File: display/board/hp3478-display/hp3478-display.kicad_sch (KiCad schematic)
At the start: 60 parts, among them J1 Header, J2 Header, U1 FT60F1x2, U2 SM16206S, U3 74HC595, U4 74HC595

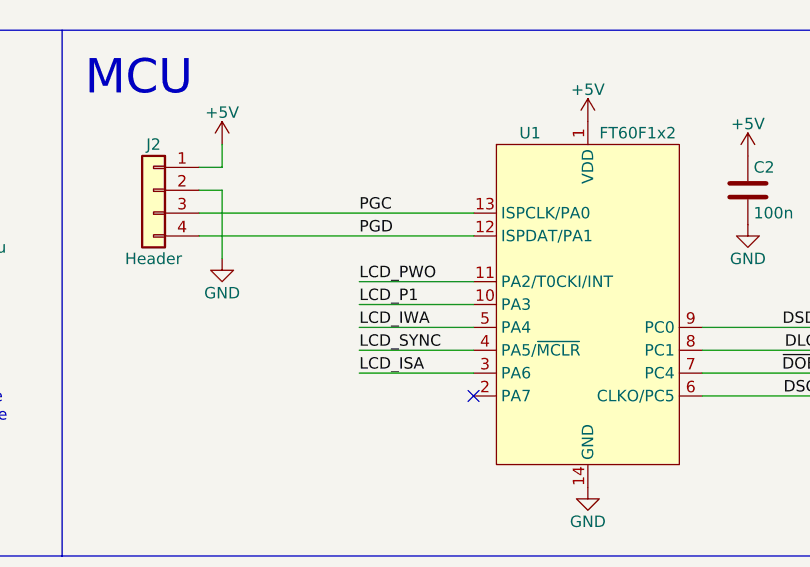
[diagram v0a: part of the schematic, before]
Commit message: Swap LCD_P1 and LCD_PWO on MCU so P1 can have edge-triggered interrupts.
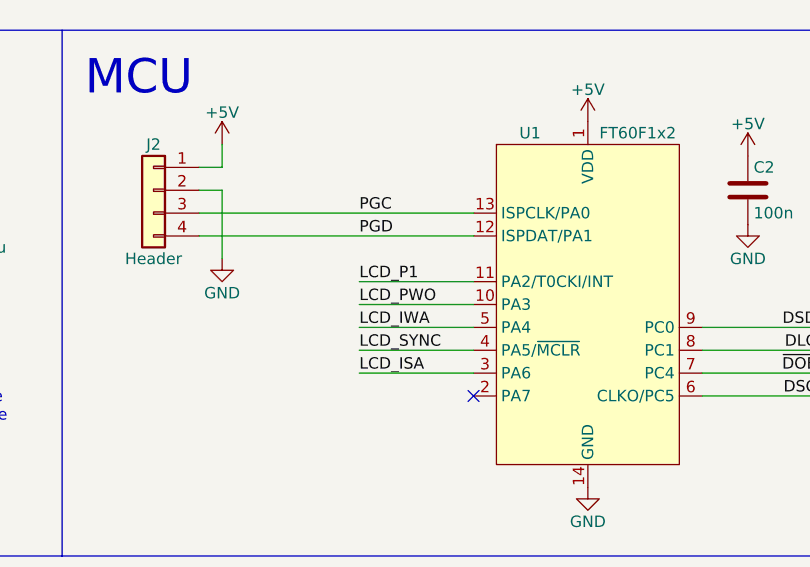
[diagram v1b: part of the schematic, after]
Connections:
- net LCD_P1: now also U1.11 (PA2/T0CKI/INT); no longer U1.10 (PA3)
- net LCD_PWO: now also U1.10 (PA3); no longer U1.11 (PA2/T0CKI/INT)
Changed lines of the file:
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@@
     (effects (font (size 1.27 1.27)) (justify right bottom))
   )
-  (label "LCD_P1" (at 109.22 111.76 0)
+  (label "LCD_P1" (at 109.22 109.22 0)
     (effects (font (size 1.27 1.27)) (justify left bottom))
   )
@@
     (effects (font (size 1.27 1.27)) (justify left bottom))
   )
-  (label "LCD_PWO" (at 109.22 109.22 0)
-    (effects (font (size 1.27 1.27)) (justify left bottom))
-  )
+  (label "LCD_PWO" (at 109.22 111.76 0)
+    (effects (font (size 1.27 1.27)) (justify left bottom))
+  )
